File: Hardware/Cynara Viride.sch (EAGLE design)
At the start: 168 parts, among them Q1 TXC-7B, Q2 TXC-7WNEO, SW1 430181038816, SW2 , T1 PDTC143, T2 PDTC143, T3 PDTC143, T4 PDTC143, T5 PDTC143, U1 TM4C129EN, U2 MCP1826S 3V3, U3 LM4132 3V3, U4 XC6SLX9-3TQG, U5 M25P16-SO8, U6 MCP1826S 1V2, X1 EDGE 50p, X11 SOCK2X17, X12 SOCK2X17, X13 SOCK2X17, X2 EDGE 50p, X23 debug xilinx, X24 debug 10p, X3 EDGE 50p, X4 EDGE 50p, X5 MicroMatch 24, X6 , X7 SOCK2X17, X8 RJ45-LAN-10/100

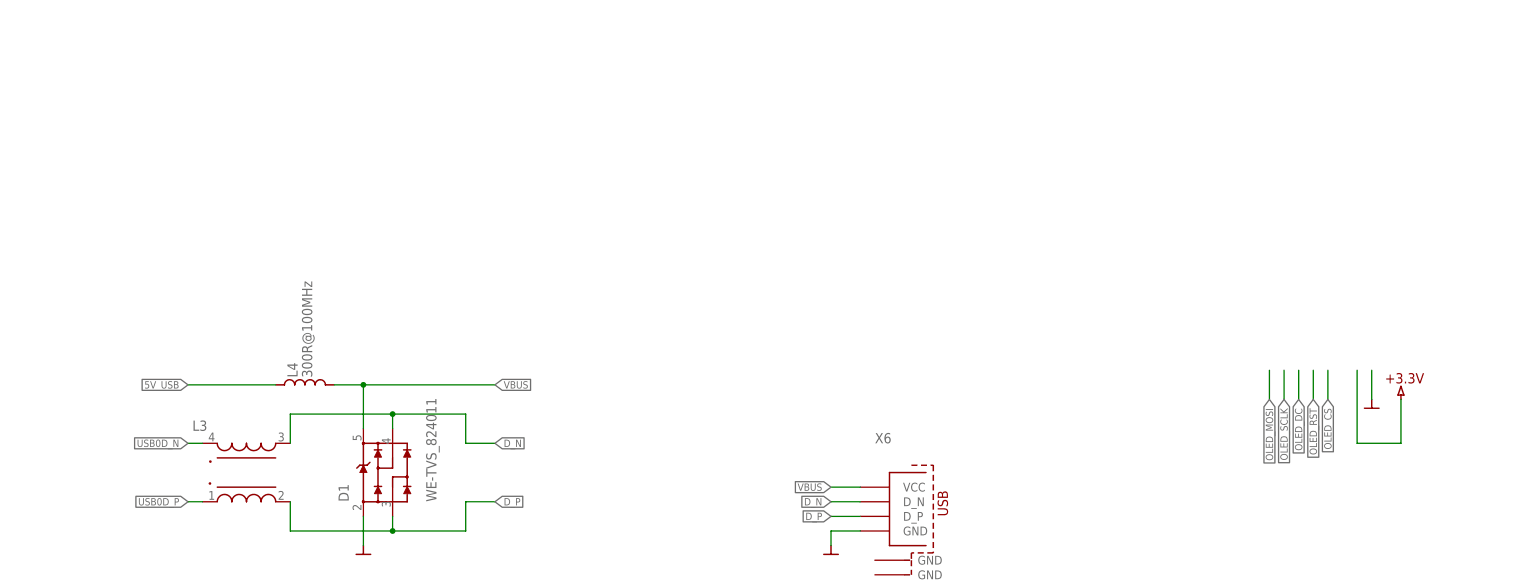
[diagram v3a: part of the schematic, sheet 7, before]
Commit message: Added VBUS detect circuitry. Drill size of mounting holes is 3.5 mm to fit M3 bolts.
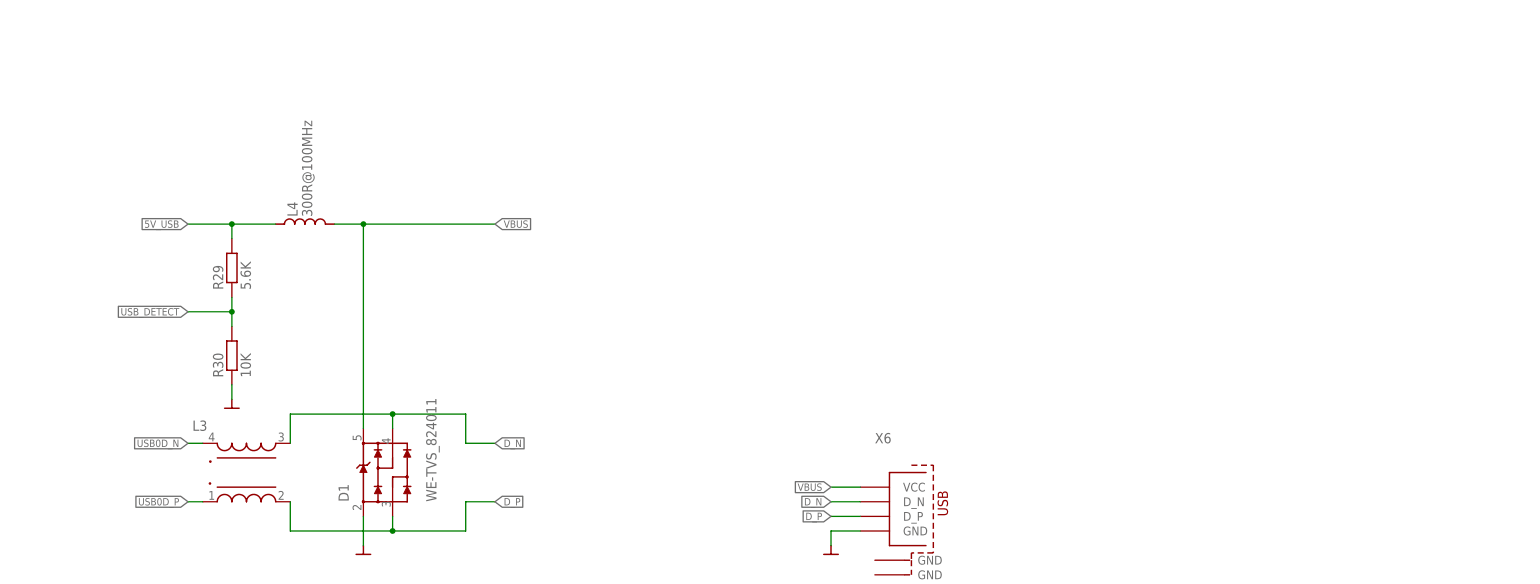
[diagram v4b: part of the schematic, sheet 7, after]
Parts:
- added R29: 5.6K, Cynara-Passives:R-EU_R0603
- added R30: 10K, Cynara-Passives:R-EU_R0603
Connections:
- removed net USB_DETECT1: U1Q.PQ4
- removed net USB_DETECT2: U1K.PK4
- new net USB_DETECT: R29.1, R30.2, U1K.PK4
- net 5V_USB: now also R29.2
- net GND: now also R30.1
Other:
- moved on the sheet: L4
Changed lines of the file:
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@@
 <setting verticaltext="up"/>
 </settings>
-<grid distance="0.1" unitdist="inch" unit="inch" style="lines" multiple="1" display="yes" altdistance="0.01" altunitdist="inch" altunit="inch"/>
+<grid distance="0.1" unitdist="inch" unit="inch" style="lines" multiple="1" display="no" altdistance="0.01" altunitdist="inch" altunit="inch"/>
 <layers>
 <layer number="1" name="Top" color="4" fill="1" visible="no" active="no"/>
@@
 <part name="U$22" library="Cynara-Symbols" deviceset="+1.2V" device=""/>
 <part name="=149" library="Cynara-Symbols" deviceset="GND" device=""/>
-<part name="=150" library="Cynara-Symbols" deviceset="GND" device=""/>
-<part name="U$23" library="Cynara-Symbols" deviceset="+3.3V" device=""/>
 <part name="C61" library="Cynara-Passives" deviceset="C-EU" device="C0603" value="100uF"/>
 <part name="=151" library="Cynara-Symbols" deviceset="GND" device=""/>
@@
 <part name="=162" library="Cynara-Symbols" deviceset="GND" device=""/>
 <part name="X6" library="Cynara-Connectors" deviceset="USB2.0" device="-TYPE-B" value=" "/>
+<part name="R29" library="Cynara-Passives" deviceset="R-EU_" device="R0603" value="5.6K"/>
+<part name="R30" library="Cynara-Passives" deviceset="R-EU_" device="R0603" value="10K"/>
+<part name="=150" library="Cynara-Symbols" deviceset="GND" device=""/>
 </parts>
 <sheets>
@@
 </segment>
 </net>
-<net name="USB_DETECT1" class="0">
+<net name="USB_DETECT" class="0">
 <segment>
-<wire x1="81.28" y1="78.74" x2="76.2" y2="78.74" width="0.1524" layer="91"/>
-<pinref part="U1" gate="Q" pin="PQ4"/>
-<label x="81.28" y="78.74" size="1.27" layer="95" xref="yes"/>
+<pinref part="U1" gate="K" pin="PK4"/>
+<wire x1="27.94" y1="129.54" x2="33.02" y2="129.54" width="0.1524" layer="91"/>
+<label x="33.02" y="129.54" size="1.27" layer="95" xref="yes"/>
 </segment>
 </net>
@@
 </segment>
 </net>
-<net name="USB_DETECT2" class="0">
-<segment>
-<pinref part="U1" gate="K" pin="PK4"/>
-<wire x1="27.94" y1="129.54" x2="33.02" y2="129.54" width="0.1524" layer="91"/>
-<label x="33.02" y="129.54" size="1.27" layer="95" xref="yes"/>
-</segment>
-</net>
 <net name="FREE" class="0">
 <segment>
@@
 <instance part="L3" gate="G$1" x="96.52" y="81.28"/>
 <instance part="D1" gate="G$1" x="121.92" y="81.28"/>
-<instance part="L4" gate="G$1" x="106.68" y="96.52" rot="R90"/>
+<instance part="L4" gate="G$1" x="106.68" y="124.46" rot="R90"/>
 <instance part="=147" gate=" " x="116.84" y="66.04"/>
-<instance part="=150" gate=" " x="292.1" y="91.44"/>
-<instance part="U$23" gate=" " x="297.18" y="96.52"/>
 <instance part="C61" gate="G$1" x="119.38" y="177.8"/>
 <instance part="=151" gate=" " x="119.38" y="167.64"/>
@@
 <instance part="=162" gate=" " x="198.12" y="66.04"/>
 <instance part="X6" gate="X1" x="213.36" y="76.2"/>
+<instance part="R29" gate="G$1" x="93.98" y="116.84" rot="R90"/>
+<instance part="R30" gate="G$1" x="93.98" y="101.6" rot="R90"/>
+<instance part="=150" gate=" " x="93.98" y="91.44"/>
 </instances>
 <busses>
@@
 <pinref part="D1" gate="G$1" pin="VDD"/>
 <pinref part="L4" gate="G$1" pin="F"/>
-<wire x1="116.84" y1="96.52" x2="116.84" y2="88.9" width="0.1524" layer="91"/>
-<wire x1="111.76" y1="96.52" x2="116.84" y2="96.52" width="0.1524" layer="91"/>
-<junction x="116.84" y="96.52"/>
-<wire x1="116.84" y1="96.52" x2="139.7" y2="96.52" width="0.1524" layer="91"/>
-<label x="139.7" y="96.52" size="1.27" layer="95" xref="yes"/>
+<wire x1="116.84" y1="124.46" x2="116.84" y2="88.9" width="0.1524" layer="91"/>
+<wire x1="111.76" y1="124.46" x2="116.84" y2="124.46" width="0.1524" layer="91"/>
+<junction x="116.84" y="124.46"/>
+<wire x1="116.84" y1="124.46" x2="139.7" y2="124.46" width="0.1524" layer="91"/>
+<label x="139.7" y="124.46" size="1.27" layer="95" xref="yes"/>
 </segment>
 <segment>
@@
 </segment>
 <segment>
-<pinref part="=150" gate=" " pin="GND"/>
-<wire x1="292.1" y1="99.06" x2="292.1" y2="93.98" width="0.1524" layer="91"/>
-</segment>
-<segment>
 <pinref part="C61" gate="G$1" pin="2"/>
 <wire x1="119.38" y1="170.18" x2="119.38" y2="172.72" width="0.1524" layer="91"/>
@@
 <wire x1="198.12" y1="71.12" x2="203.2" y2="71.12" width="0.1524" layer="91"/>
 </segment>
+<segment>
+<pinref part="R30" gate="G$1" pin="1"/>
+<pinref part="=150" gate=" " pin="GND"/>
+<wire x1="93.98" y1="96.52" x2="93.98" y2="93.98" width="0.1524" layer="91"/>
+</segment>
 </net>
 <net name="USB0D_N" class="0">
@@
 <net name="+3.3V" class="0">
 <segment>
-<pinref part="U$23" gate=" " pin="+3.3V"/>
-<wire x1="289.56" y1="86.36" x2="297.18" y2="86.36" width="0.1524" layer="91"/>
-<wire x1="297.18" y1="86.36" x2="297.18" y2="93.98" width="0.1524" layer="91"/>
-<wire x1="289.56" y1="99.06" x2="289.56" y2="86.36" width="0.1524" layer="91"/>
-</segment>
-<segment>
 <wire x1="119.38" y1="195.58" x2="119.38" y2="180.34" width="0.1524" layer="91"/>
 <pinref part="C61" gate="G$1" pin="1"/>
@@
 </segment>
 </net>
-<net name="OLED_MOSI" class="0">
-<segment>
-<wire x1="274.32" y1="99.06" x2="274.32" y2="93.98" width="0.1524" layer="91"/>
-<label x="274.32" y="93.98" size="1.27" layer="95" rot="R270" xref="yes"/>
-</segment>
-</net>
-<net name="OLED_SCLK" class="0">
-<segment>
-<wire x1="276.86" y1="99.06" x2="276.86" y2="93.98" width="0.1524" layer="91"/>
-<label x="276.86" y="93.98" size="1.27" layer="95" rot="R270" xref="yes"/>
-</segment>
-</net>
-<net name="OLED_DC" class="0">
-<segment>
-<wire x1="279.4" y1="99.06" x2="279.4" y2="93.98" width="0.1524" layer="91"/>
-<label x="279.4" y="93.98" size="1.27" layer="95" rot="R270" xref="yes"/>
-</segment>
-</net>
-<net name="OLED_RST" class="0">
-<segment>
-<wire x1="281.94" y1="99.06" x2="281.94" y2="93.98" width="0.1524" layer="91"/>
-<label x="281.94" y="93.98" size="1.27" layer="95" rot="R270" xref="yes"/>
-</segment>
-</net>
-<net name="OLED_CS" class="0">
-<segment>
-<wire x1="284.48" y1="99.06" x2="284.48" y2="93.98" width="0.1524" layer="91"/>
-<label x="284.48" y="93.98" size="1.27" layer="95" rot="R270" xref="yes"/>
-</segment>
-</net>
 <net name="5V_USB" class="0">
 <segment>
 <pinref part="L4" gate="G$1" pin="E"/>
-<wire x1="101.6" y1="96.52" x2="86.36" y2="96.52" width="0.1524" layer="91"/>
-<label x="86.36" y="96.52" size="1.27" layer="95" rot="R180" xref="yes"/>
+<wire x1="101.6" y1="124.46" x2="93.98" y2="124.46" width="0.1524" layer="91"/>
+<label x="86.36" y="124.46" size="1.27" layer="95" rot="R180" xref="yes"/>
+<pinref part="R29" gate="G$1" pin="2"/>
+<wire x1="93.98" y1="124.46" x2="86.36" y2="124.46" width="0.1524" layer="91"/>
+<wire x1="93.98" y1="121.92" x2="93.98" y2="124.46" width="0.1524" layer="91"/>
+<junction x="93.98" y="124.46"/>
 </segment>
 </net>
@@
 </segment>
 </net>
+<net name="USB_DETECT" class="0">
+<segment>
+<pinref part="R29" gate="G$1" pin="1"/>
+<pinref part="R30" gate="G$1" pin="2"/>
+<wire x1="93.98" y1="111.76" x2="93.98" y2="109.22" width="0.1524" layer="91"/>
+<wire x1="93.98" y1="109.22" x2="93.98" y2="106.68" width="0.1524" layer="91"/>
+<wire x1="93.98" y1="109.22" x2="86.36" y2="109.22" width="0.1524" layer="91"/>
+<junction x="93.98" y="109.22"/>
+<label x="86.36" y="109.22" size="1.27" layer="95" rot="R180" xref="yes"/>
+</segment>
+</net>

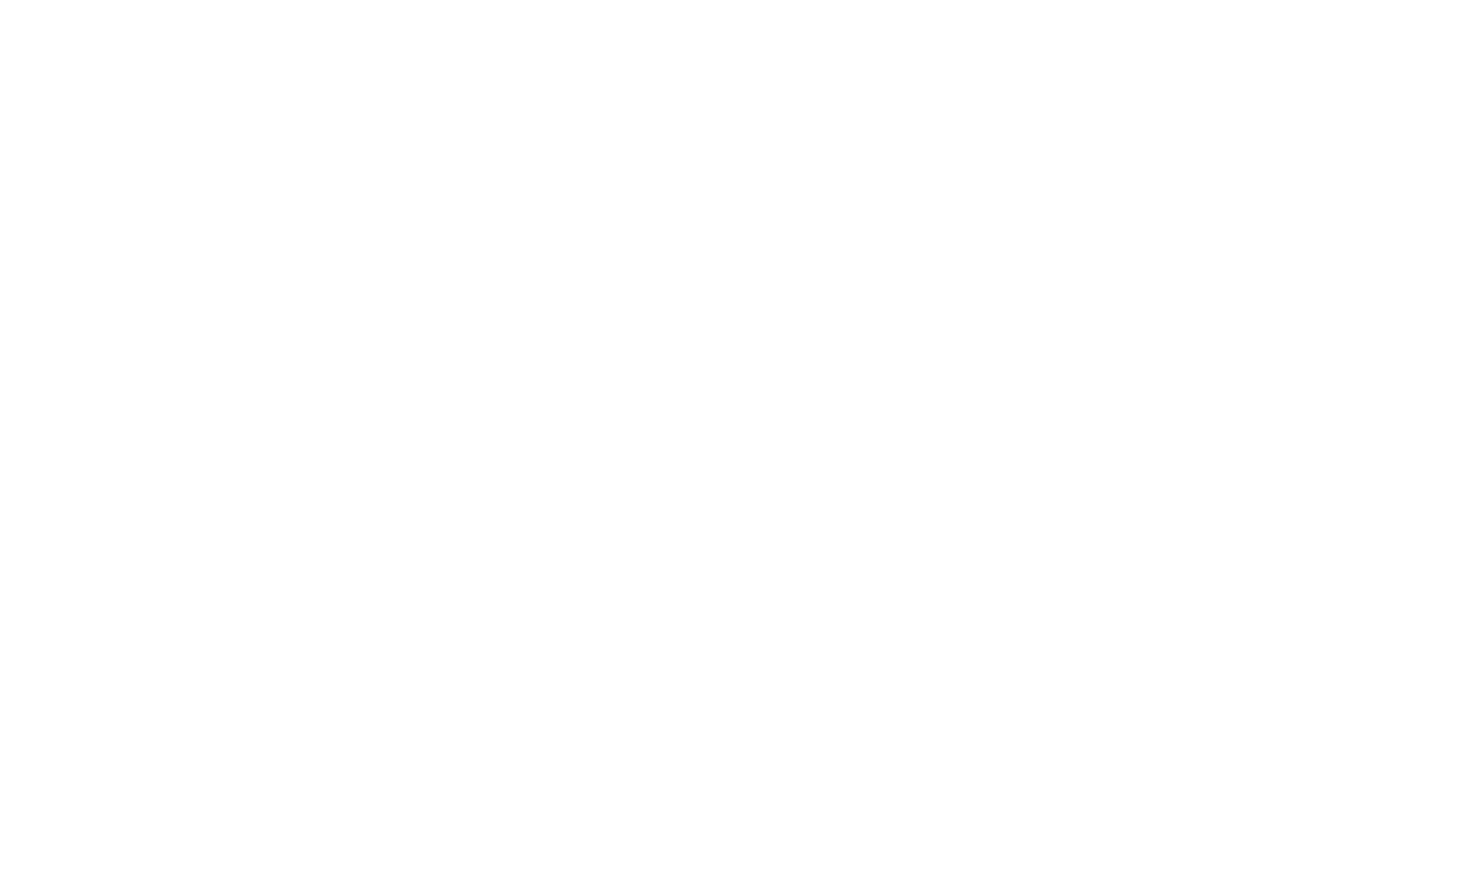
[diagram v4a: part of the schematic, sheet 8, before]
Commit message: Proper mounting holes. Small change in layout of +1.2V plane. Enhanced USB connector symbol. Added shield conenctions.
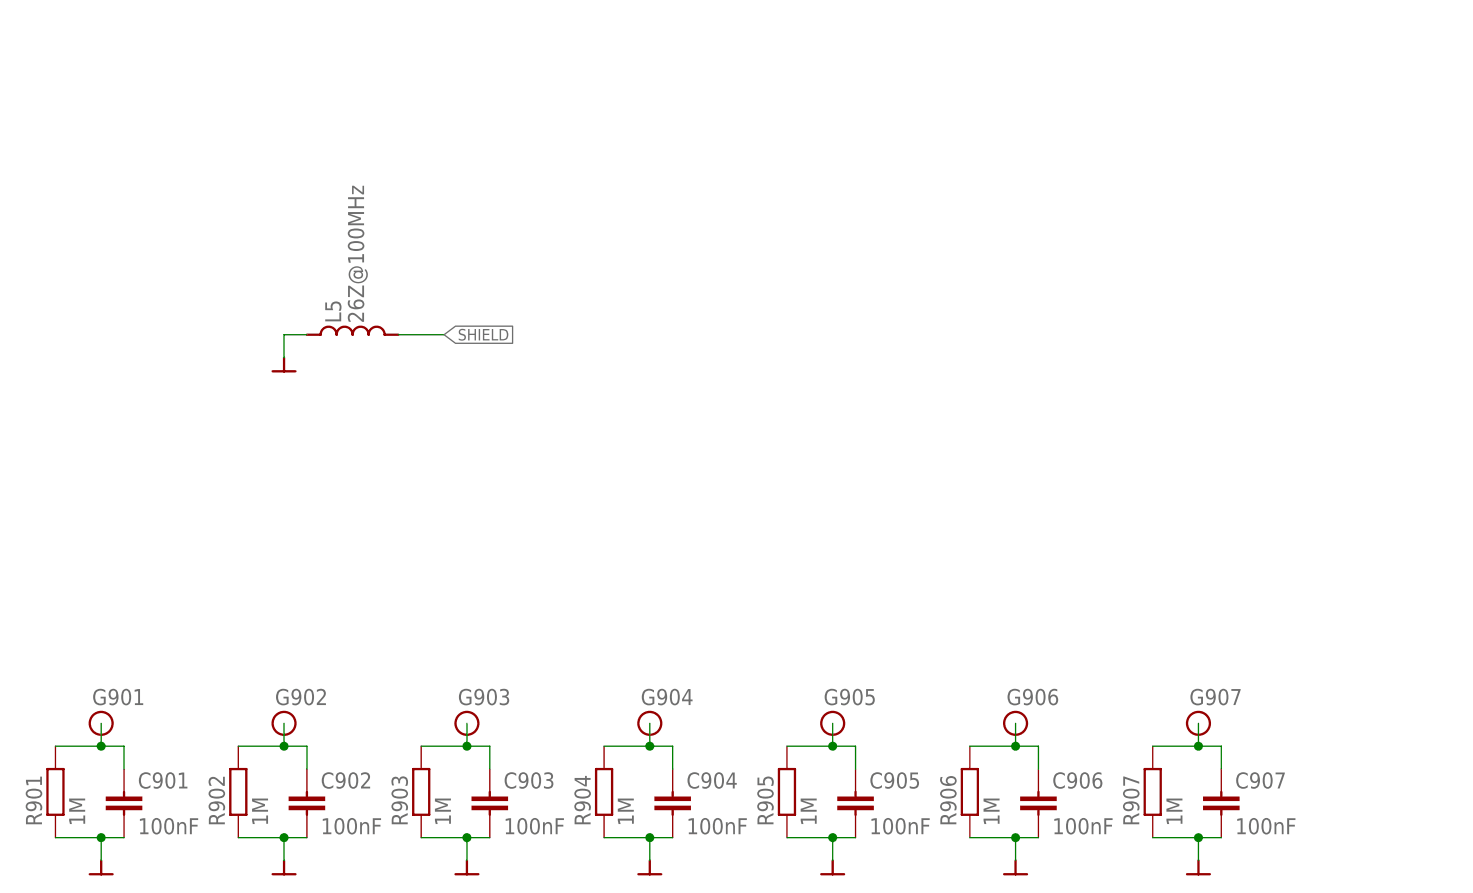
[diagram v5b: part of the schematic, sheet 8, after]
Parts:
- added C901, C902, C903, C904, C905, C906, C907: 100nF, Cynara-Passives:C-EUC0603
- added G901, G902, G903, G904, G905, G906, G907: (no value), Cynara-Misc:HOLE=3,5/6,6
- added L5: 26Z@100MHz, Cynara-Passives:BEAD_26Z@100MHZ[0603]
- added R901, R902, R903, R904, R905, R906, R907: 1M, Cynara-Passives:R-EU_R0603
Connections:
- new net G901: C901.1, G901.1, R901.2
- new net G902: C902.1, G902.1, R902.2
- new net G903: C903.1, G903.1, R903.2
- new net G904: C904.1, G904.1, R904.2
- new net G905: C905.1, G905.1, R905.2
- new net G906: C906.1, G906.1, R906.2
- new net G907: C907.1, G907.1, R907.2
- new net SHIELD: L5.F, X6.GND@1, X6.GND@2, X8-SHIELD.P$1
- net GND: now also C901.2, C902.2, C903.2, C904.2, C905.2, C906.2, C907.2, L5.E, R901.1, R902.1, R903.1, R904.1, R905.1, R906.1, R907.1
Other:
- moved on the sheet: X8-SHIELD
